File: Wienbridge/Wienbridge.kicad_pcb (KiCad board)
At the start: 2 copper layers, 40.5 x 30.9 mm, 24 parts, among them J1 OUTPUT, J2 PWR switch, U4 NE5532, U5 NE5532

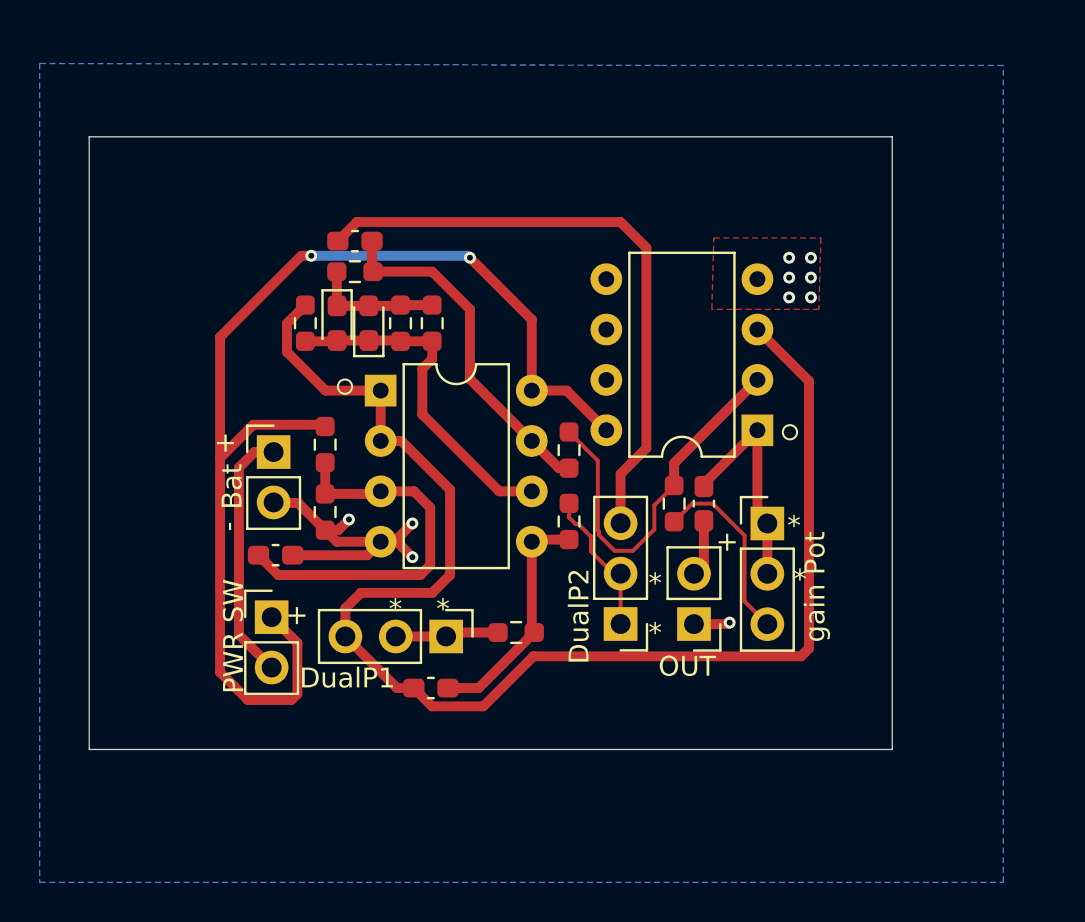
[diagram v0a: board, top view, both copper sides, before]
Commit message: few additions to the wein-brdige circuit and finished first revision of the opamp distortion schematic
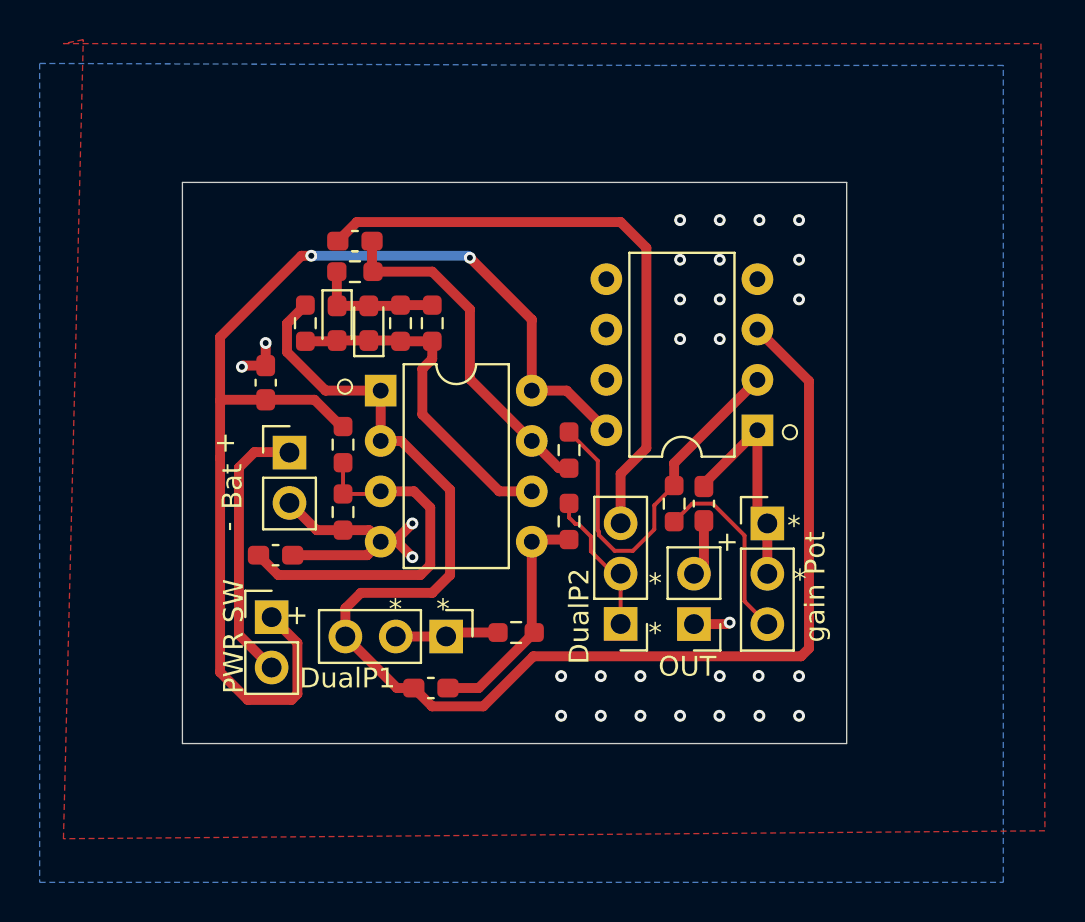
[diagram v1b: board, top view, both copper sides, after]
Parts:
- added C5: 1u?, Capacitor_SMD:C_0603_1608Metric_Pad1.08x0.95mm_HandSolder, F.Cu at (110.1, 114.2)
- moved R5 0.90 mm to (114.0, 117.3)
- moved R6 0.90 mm to (114.0, 120.7)
- moved BT1 0.80 mm to (111.3, 117.7)
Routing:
- net Net-(U4A-+): track 19.5 -> 18.6 mm
- net +9V: track 58.9 -> 59.6 mm
- net SupplyGND: track 18.1 -> 18.2 mm, vias 10 -> 30
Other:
- board size 40.5 x 30.9 mm -> 33.5 x 28.3 mm
